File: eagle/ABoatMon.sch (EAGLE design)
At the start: 30 parts, among them J1 VUSB, J2 GND, J3 GND, J4 LIPO, X1 MKDSN1,5/2-5,08

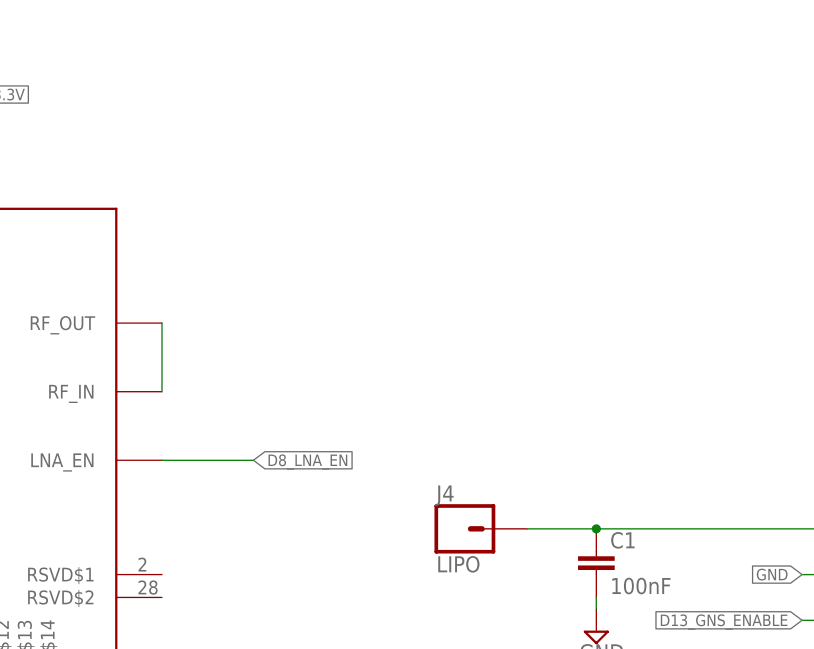
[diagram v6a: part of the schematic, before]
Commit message: added u.ft, moved GNS
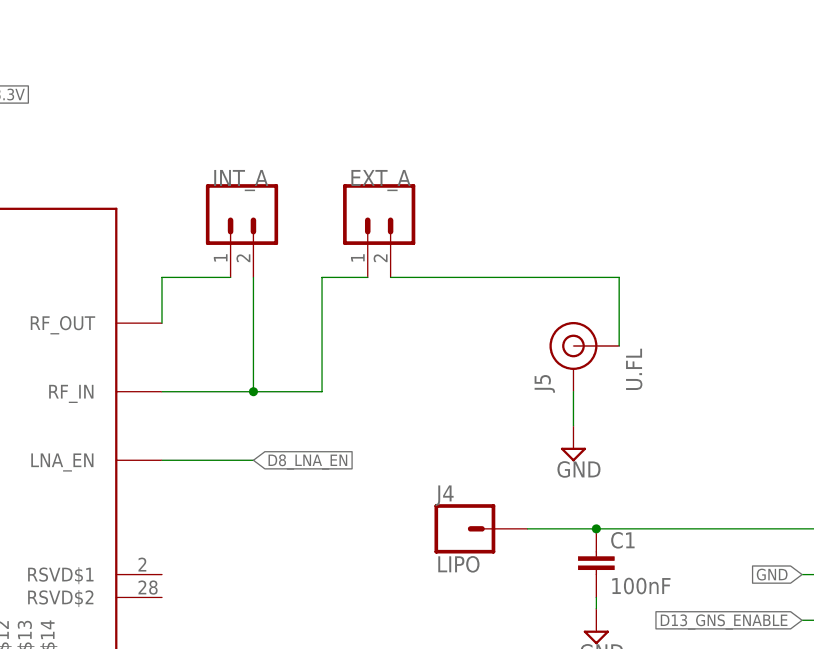
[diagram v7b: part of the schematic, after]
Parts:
- removed U$2, U$4: MOUNTINGHOLE2.5, microbuilder:MOUNTINGHOLE2.5
- added EXT_A, INT_A: (no value), SparkFun-Connectors:CONN_02
- added J5: U.FL, SparkFun-Connectors:U.FL2PIN
- added U$3, U$9: MOUNTINGHOLE2.0, microbuilder:MOUNTINGHOLE2.0
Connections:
- new net N$6: EXT_A.2, J5.SIGNAL
- new net N$7: INT_A.1, U$5.RF_OUT
- net GND: now also J5.GND
- net N$5: now also EXT_A.1, INT_A.2; no longer U$5.RF_OUT
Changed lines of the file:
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@@
 <part name="J2" library="SparkFun-Connectors" deviceset="CONN_01" device="" value="GND"/>
 <part name="J3" library="SparkFun-Connectors" deviceset="CONN_01" device="" value="GND"/>
-<part name="U$2" library="microbuilder" deviceset="MOUNTINGHOLE" device="2.5"/>
-<part name="U$4" library="microbuilder" deviceset="MOUNTINGHOLE" device="2.5"/>
 <part name="VCC" library="microbuilder" deviceset="HEADER-1X2" device="ROUND" value="JUMPER"/>
 <part name="U$1" library="microbuilder" deviceset="MOUNTINGHOLE" device="2.5"/>
@@
 <part name="SIM7020" library="SparkFun-Connectors" library_urn="urn:adsk.eagle:library:513" deviceset="CONN_07" device="" package3d_urn="urn:adsk.eagle:package:38129/1" value="SIMCOM"/>
 <part name="J4" library="SparkFun-Connectors" deviceset="CONN_01" device="" value="LIPO"/>
+<part name="U$3" library="microbuilder" deviceset="MOUNTINGHOLE" device="2.0"/>
+<part name="U$9" library="microbuilder" deviceset="MOUNTINGHOLE" device="2.0"/>
+<part name="J5" library="SparkFun-Connectors" library_urn="urn:adsk.eagle:library:513" deviceset="U.FL2PIN" device="" package3d_urn="urn:adsk.eagle:package:38237/1" value="U.FL"/>
+<part name="SUPPLY1" library="supply2" library_urn="urn:adsk.eagle:library:372" deviceset="GND" device=""/>
+<part name="INT_A" library="SparkFun-Connectors" library_urn="urn:adsk.eagle:library:513" deviceset="CONN_02" device="" package3d_urn="urn:adsk.eagle:package:38039/1"/>
+<part name="EXT_A" library="SparkFun-Connectors" library_urn="urn:adsk.eagle:library:513" deviceset="CONN_02" device="" package3d_urn="urn:adsk.eagle:package:38039/1"/>
 </parts>
 <sheets>
@@
 <attribute name="NAME" x="241.3" y="52.832" size="1.778" layer="95" font="vector" rot="R180"/>
 </instance>
-<instance part="U$2" gate="G$1" x="154.94" y="15.24" smashed="yes"/>
-<instance part="U$4" gate="G$1" x="170.18" y="15.24" smashed="yes"/>
 <instance part="VCC" gate="G$1" x="195.58" y="88.9" smashed="yes">
 <attribute name="NAME" x="189.23" y="94.615" size="1.778" layer="95"/>
 <attribute name="VALUE" x="189.23" y="83.82" size="1.778" layer="96"/>
 </instance>
-<instance part="U$1" gate="G$1" x="154.94" y="7.62" smashed="yes"/>
+<instance part="U$1" gate="G$1" x="170.18" y="15.24" smashed="yes"/>
 <instance part="GND" gate="G$1" x="162.56" y="7.62" smashed="yes"/>
 <instance part="U$7" gate="G$1" x="170.18" y="7.62" smashed="yes"/>
@@
 <attribute name="VALUE" x="142.24" y="38.354" size="1.778" layer="96" font="vector"/>
 <attribute name="NAME" x="142.24" y="46.228" size="1.778" layer="95" font="vector"/>
+</instance>
+<instance part="U$3" gate="G$1" x="154.94" y="15.24" smashed="yes"/>
+<instance part="U$9" gate="G$1" x="154.94" y="7.62" smashed="yes"/>
+<instance part="J5" gate="G$1" x="157.48" y="63.5" smashed="yes">
+<attribute name="NAME" x="154.94" y="58.42" size="1.778" layer="95" rot="R90"/>
+<attribute name="VALUE" x="165.1" y="58.42" size="1.778" layer="96" rot="R90"/>
+</instance>
+<instance part="SUPPLY1" gate="GND" x="157.48" y="52.07" smashed="yes">
+<attribute name="VALUE" x="155.575" y="48.895" size="1.778" layer="96"/>
+</instance>
+<instance part="INT_A" gate="G$1" x="119.38" y="78.74" smashed="yes" rot="R270">
+<attribute name="VALUE" x="114.554" y="81.28" size="1.778" layer="96" font="vector" rot="R270"/>
+<attribute name="NAME" x="117.348" y="81.28" size="1.778" layer="95" font="vector"/>
+</instance>
+<instance part="EXT_A" gate="G$1" x="134.62" y="78.74" smashed="yes" rot="R270">
+<attribute name="VALUE" x="129.794" y="81.28" size="1.778" layer="96" font="vector" rot="R270"/>
+<attribute name="NAME" x="132.588" y="81.28" size="1.778" layer="95" font="vector"/>
 </instance>
 </instances>
@@
 <label x="162.56" y="139.7" size="1.27" layer="95" xref="yes"/>
 </segment>
+<segment>
+<pinref part="J5" gate="G$1" pin="GND"/>
+<pinref part="SUPPLY1" gate="GND" pin="GND"/>
+<wire x1="157.48" y1="58.42" x2="157.48" y2="54.61" width="0.1524" layer="91"/>
+</segment>
 </net>
 <net name="VUSB" class="1">
@@
 </segment>
 </net>
-<net name="N$5" class="0">
-<segment>
-<pinref part="U$5" gate="G$1" pin="RF_OUT"/>
-<pinref part="U$5" gate="G$1" pin="RF_IN"/>
-<wire x1="111.76" y1="66.04" x2="111.76" y2="58.42" width="0.1524" layer="91"/>
-</segment>
-</net>
 <net name="GNS_VCC" class="2">
 <segment>
@@
 </segment>
 </net>
+<net name="N$6" class="1">
+<segment>
+<pinref part="J5" gate="G$1" pin="SIGNAL"/>
+<wire x1="162.56" y1="63.5" x2="162.56" y2="71.12" width="0.1524" layer="91"/>
+<pinref part="EXT_A" gate="G$1" pin="2"/>
+<wire x1="162.56" y1="71.12" x2="137.16" y2="71.12" width="0.1524" layer="91"/>
+</segment>
+</net>
+<net name="N$5" class="2">
+<segment>
+<pinref part="EXT_A" gate="G$1" pin="1"/>
+<wire x1="134.62" y1="71.12" x2="129.54" y2="71.12" width="0.1524" layer="91"/>
+<wire x1="129.54" y1="71.12" x2="129.54" y2="58.42" width="0.1524" layer="91"/>
+<pinref part="U$5" gate="G$1" pin="RF_IN"/>
+<wire x1="129.54" y1="58.42" x2="121.92" y2="58.42" width="0.1524" layer="91"/>
+<pinref part="INT_A" gate="G$1" pin="2"/>
+<wire x1="121.92" y1="58.42" x2="111.76" y2="58.42" width="0.1524" layer="91"/>
+<wire x1="121.92" y1="71.12" x2="121.92" y2="58.42" width="0.1524" layer="91"/>
+<junction x="121.92" y="58.42"/>
+</segment>
+</net>
+<net name="N$7" class="2">
+<segment>
+<pinref part="U$5" gate="G$1" pin="RF_OUT"/>
+<pinref part="INT_A" gate="G$1" pin="1"/>
+<wire x1="111.76" y1="66.04" x2="111.76" y2="71.12" width="0.1524" layer="91"/>
+<wire x1="111.76" y1="71.12" x2="119.38" y2="71.12" width="0.1524" layer="91"/>
+</segment>
+</net>

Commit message: errors cleared
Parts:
- removed U$8: MOUNTINGHOLE2.5, microbuilder:MOUNTINGHOLE2.5
- added JST1: (no value), SparkFun-Connectors:CONN_09
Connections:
- removed net D12_TIMEPULSE: D1.C
- removed net D8_LNA_EN: U$5.LNA_EN, U$6.D8
- new net D14_LNA_EN: U$5.LNA_EN, U$6.A0_DAC
- new net D17_TIMEPULSE: D1.C, U$6.A3
- new net D18: JST1.8, U$6.A4
- new net D2: JST1.9, U$6.D2
- new net MISO: JST1.5, U$6.MISO
- new net MOSI: JST1.7, U$6.MOSI
- new net SCK: JST1.6, U$6.SCK
- new net SCL: JST1.2, U$6.SCL
- new net SDA: JST1.4, U$6.SDA
- net 3.3V: now also U$6.3V3
- net GND: now also JST1.1, JST1.3
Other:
- note added: "VCC / GND Screw connector"
- note removed: "VCC / GND Screw connection"
- moved on the sheet: JST, R1, R7, SIM7020
